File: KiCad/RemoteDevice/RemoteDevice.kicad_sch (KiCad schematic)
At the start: 42 parts, among them J1 CN1, J2 Antenne, Q1 Si4435, SW1 SW_MEC_5E, SW2 SW_MEC_5E, U1 STM32L041F6Px, U2 XC9140, U3 MCP6281, U4 ADT7410TRZ, U5 MCP6281, U6 RT606

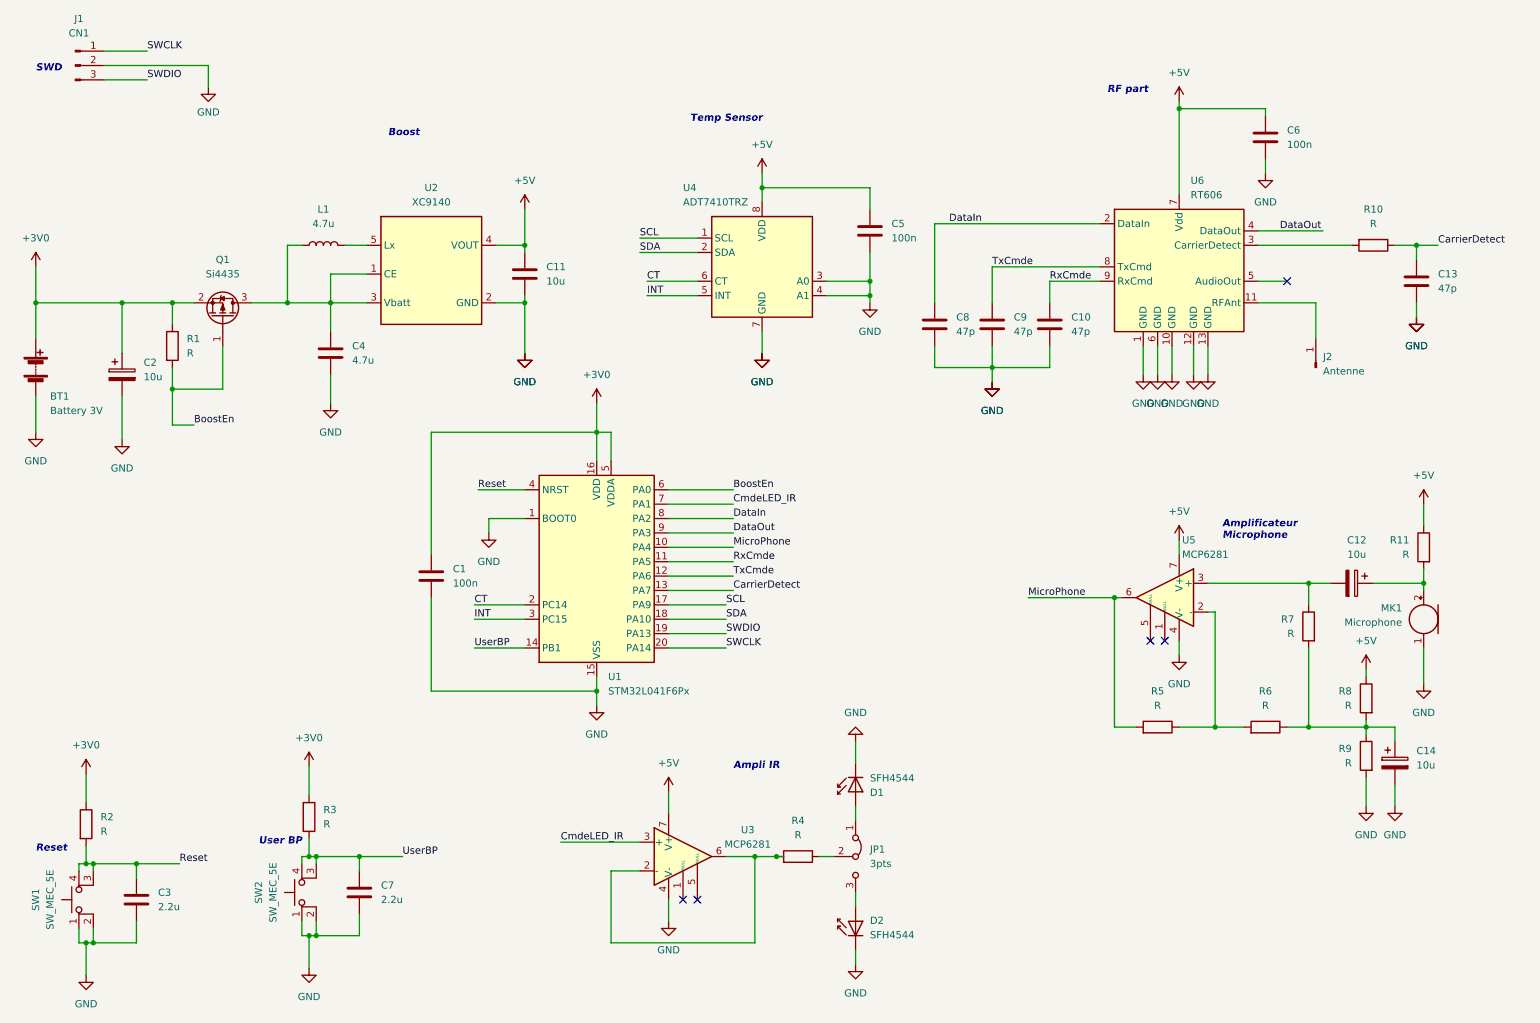
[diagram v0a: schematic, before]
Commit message: Edge cut OK, le compartiment de pile ne fait pas partie du brd (car pb en épaisseur). Placement commencé
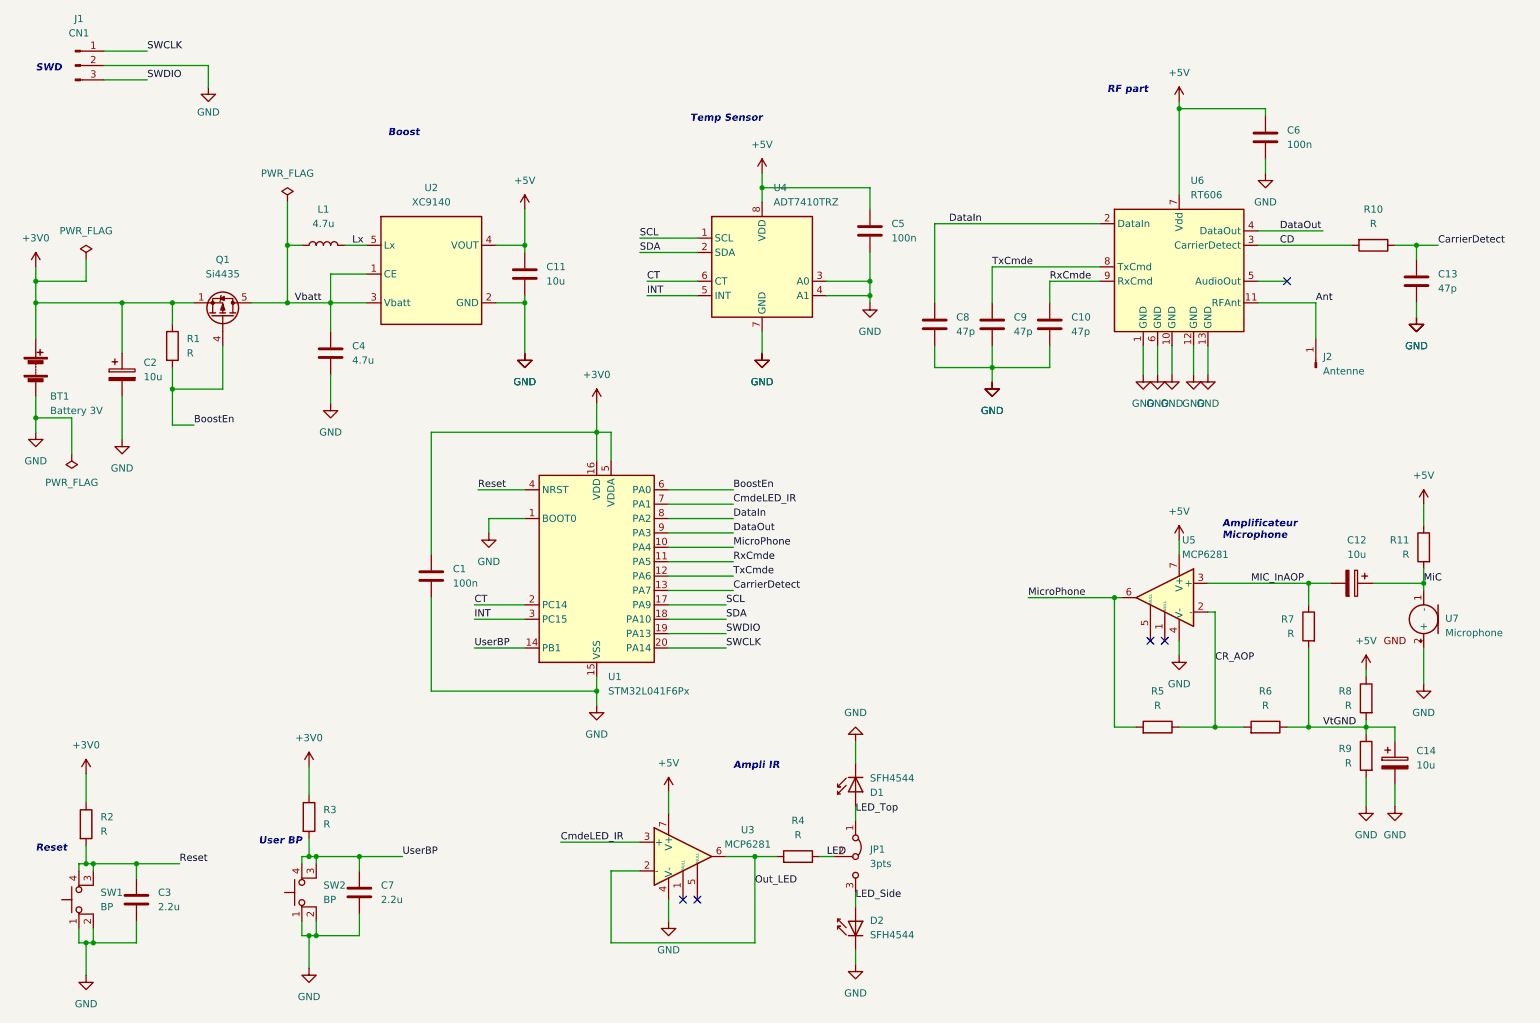
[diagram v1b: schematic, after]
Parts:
- removed MK1: Microphone, symbol Device:Microphone
- removed Q1: Si4435, symbol Device:Q_PMOS_GSD
- removed SW1, SW2: SW_MEC_5E, symbol Switch:SW_MEC_5E
- removed U2: XC9140, Package_TO_SOT_SMD:SOT-23-5, symbol ProjDeviceManag_PV:XC9140
- removed U4: ADT7410TRZ, Package_SO:SOP-8_3.9x4.9mm_P1.27mm, symbol ProjDeviceManag_PV:ADT7410TRZ
- removed U6: RT606, ProjDeviceManag_PV:RT606, symbol ProjDeviceManag_PV:RT606
- added Q1: Si4435, Package_SO:PowerPAK_SO-8_Single, symbol Transistor_FET:Si7141DP
- added SW1, SW2: BP, LibKiCad_PjtDeviceManagePV:SW, symbol LibKiCad_PjtDeviceManagePV:SwitchBP
- added U2: XC9140, Package_TO_SOT_SMD:SOT-23-5, symbol LibKiCad_PjtDeviceManagePV:XC9140
- added U4: ADT7410TRZ, Package_SO:SOP-8_3.9x4.9mm_P1.27mm, symbol LibKiCad_PjtDeviceManagePV:ADT7410TRZ
- added U6: RT606, LibKiCad_PjtDeviceManagePV:RT606, symbol LibKiCad_PjtDeviceManagePV:RT606
- added U7: Microphone, LibKiCad_PjtDeviceManagePV:Microphone, symbol LibKiCad_PjtDeviceManagePV:Microphone
- U3, U5: footprint (none) -> Package_SO:SOIC-8_3.9x4.9mm_P1.27mm
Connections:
- net +3V0: now also Q1.1 (S), Q1.2 (S), Q1.3 (S)
- net +5V: now also U2.4 (VOUT), U4.8 (VDD), U6.7 (Vdd)
- net BoostEn: now also Q1.4 (G)
- net CT: now also U4.6 (CT)
- net DataIn: now also U6.2 (DataIn)
- net DataOut: now also U6.4 (DataOut)
- net GND: now also SW1.1, SW1.2, SW2.1, SW2.2, U2.2 (GND), U4.3 (A0), U4.4 (A1), U4.7 (GND), U6.1 (GND), U6.10 (GND), U6.12 (GND), U6.13 (GND), U6.6 (GND), U7.2 (+)
- net INT: now also U4.5 (INT)
- net Reset: now also SW1.3, SW1.4
- net RxCmde: now also U6.9 (RxCmd)
- net SCL: now also U4.1 (SCL)
- net SDA: now also U4.2 (SDA)
- net TxCmde: now also U6.8 (TxCmd)
- net UserBP: now also SW2.3, SW2.4
- net LED: now reaches JP1.2 (C), R4.1
- net Out_LED: now reaches R4.2, U3.2 (-), U3.6
- net VtGND: now reaches C14.1, R6.1, R7.2, R8.2, R9.1
- net Vbatt: now reaches C4.1, L1.2
- net Vbatt: now also Q1.5 (D), U2.1 (CE), U2.3 (Vbatt)
- net Lx: now reaches L1.1
- net Lx: now also U2.5 (Lx)
- net MiC: now reaches C12.1, R11.2
- net MiC: now also U7.1 (-)
- net LED_Top: now reaches D1.2 (A), JP1.1 (A)
- net LED_Side: now reaches D2.2 (A), JP1.3 (B)
- net Ant: now reaches J2.1 (Pin_1)
- net Ant: now also U6.11 (RFAnt)
- net CD: now reaches R10.2
- net CD: now also U6.3 (CarrierDetect)
- net CR_AOP: now reaches R5.1, R6.2, U5.2 (-)
- net MIC_InAOP: now reaches C12.2, R7.1, U5.3 (+)

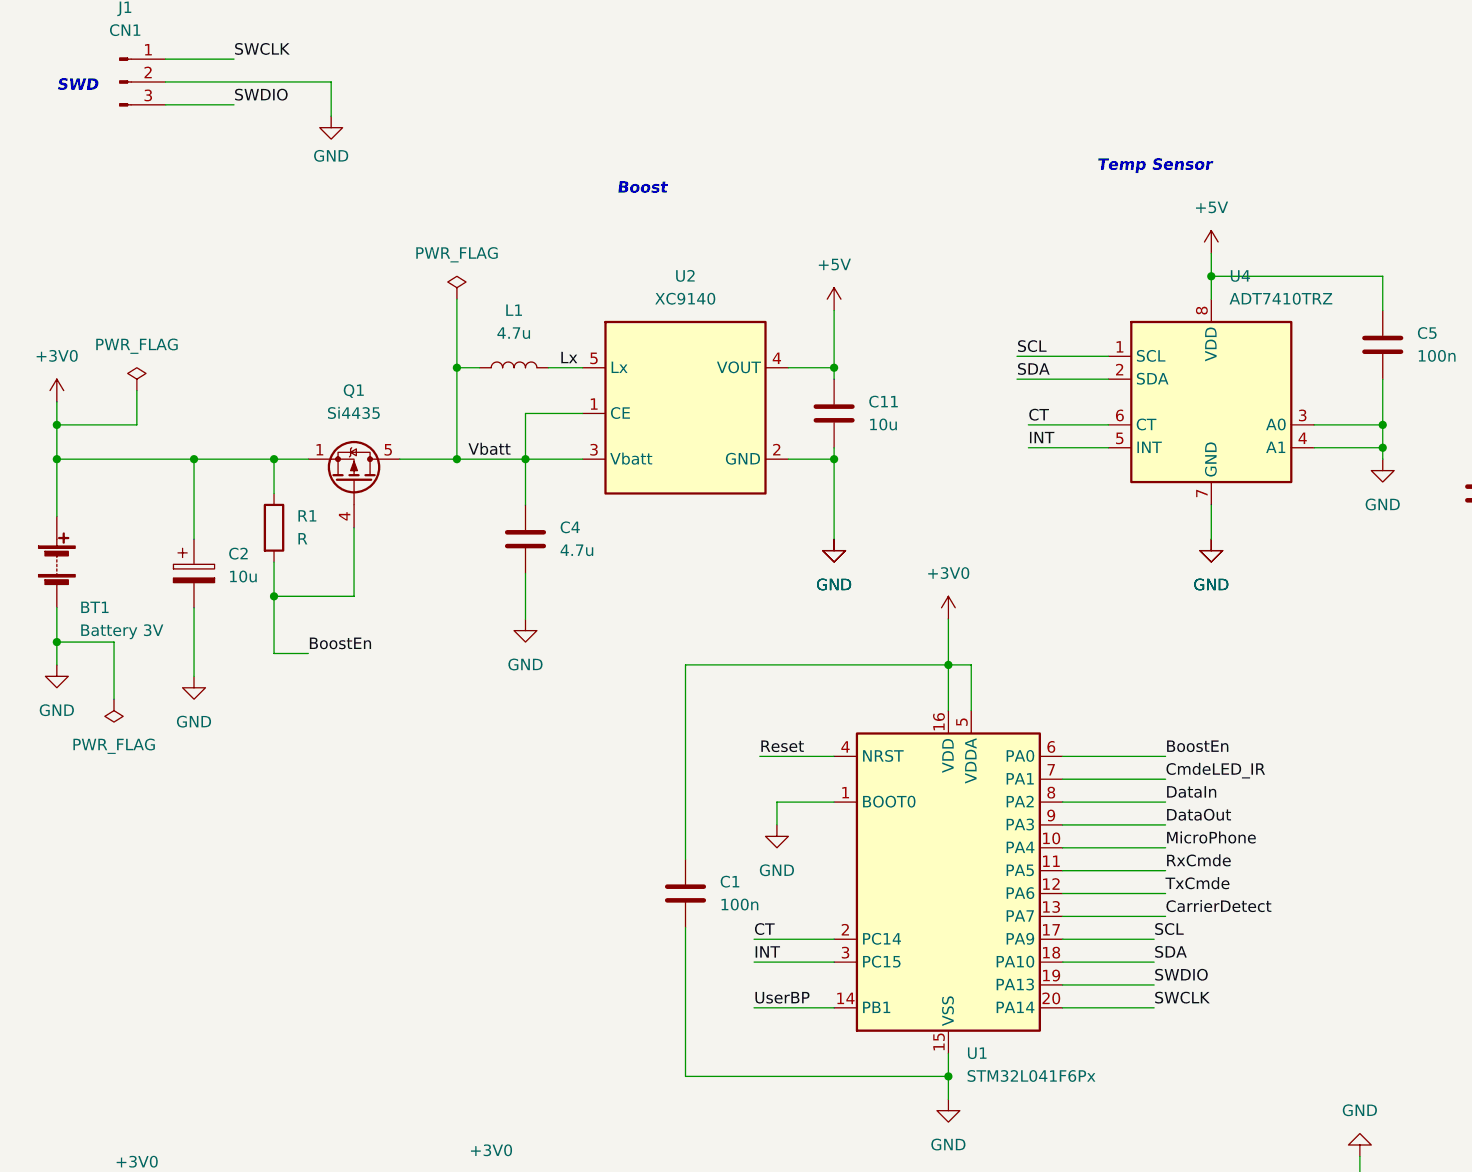
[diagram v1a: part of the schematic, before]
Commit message: routage bien avancé. Vérifier remap harmoniser odt. Reprendre pack RT606 pour passer cuivre entre pastille
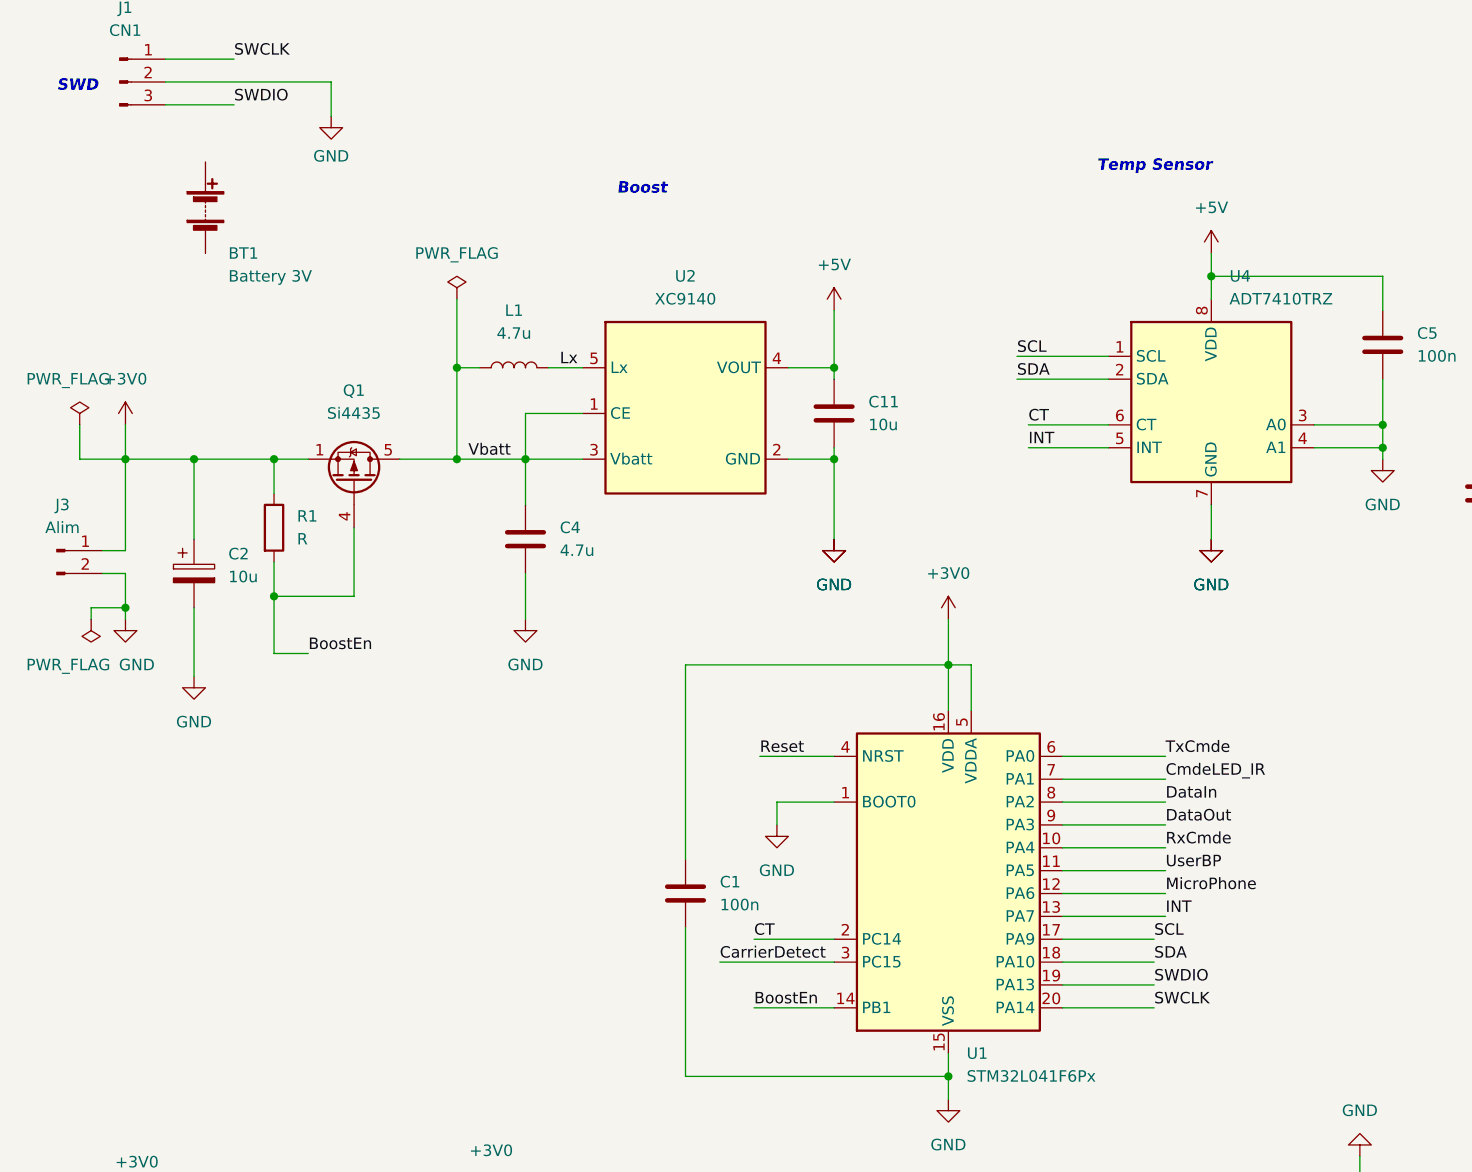
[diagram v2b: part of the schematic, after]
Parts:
- added J3: Alim, LibKiCad_PjtDeviceManagePV:PinHeader2pts, symbol Connector:Conn_01x02_Male
- J1, JP1: footprint Connector_PinHeader_2.54mm:PinHeader_1x03_P2.54mm_Vertical -> LibKiCad_PjtDeviceManagePV:PinHeader3pts
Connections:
- net +3V0: now also J3.1 (Pin_1); no longer BT1.1 (+)
- net BoostEn: now also U1.14 (PB1); no longer U1.6 (PA0)
- net CarrierDetect: now also U1.3 (PC15); no longer U1.13 (PA7)
- net GND: now also J3.2 (Pin_2); no longer BT1.2 (-)
- net INT: now also U1.13 (PA7); no longer U1.3 (PC15)
- net MicroPhone: now also U1.12 (PA6); no longer U1.10 (PA4)
- net RxCmde: now also U1.10 (PA4); no longer U1.11 (PA5)
- net TxCmde: now also U1.6 (PA0); no longer U1.12 (PA6)
- net UserBP: now also U1.11 (PA5); no longer U1.14 (PB1)
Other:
- moved on the sheet: BT1

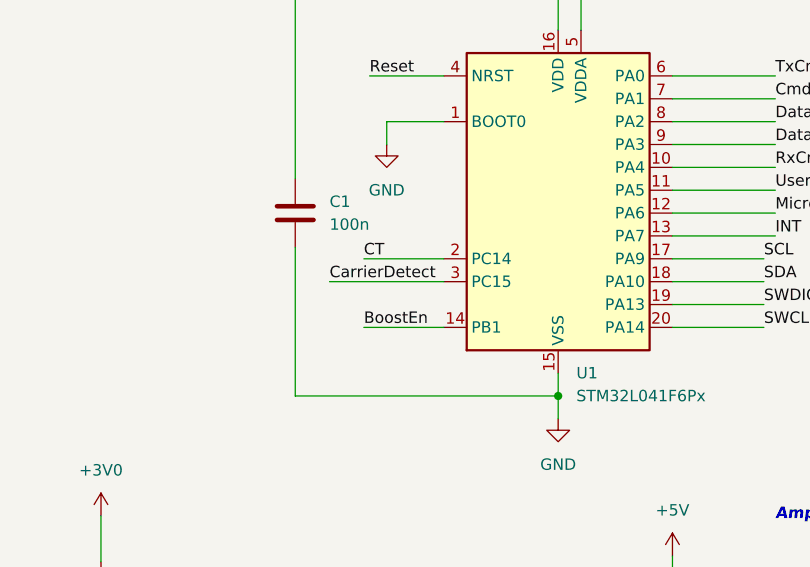
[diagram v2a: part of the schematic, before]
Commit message: paxkagez RT606 OK, remap à contrôler, routage presque entièrement dégrossi, pb DRC sur edge cut
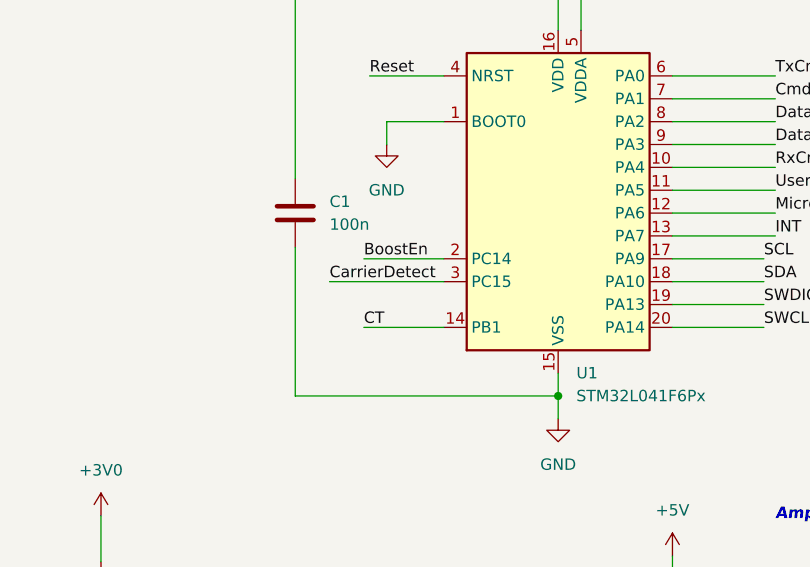
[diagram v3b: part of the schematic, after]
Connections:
- net BoostEn: now also U1.2 (PC14); no longer U1.14 (PB1)
- net CT: now also U1.14 (PB1); no longer U1.2 (PC14)
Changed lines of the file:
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@@
     (effects (font (size 1.27 1.27)) (justify left bottom))
   )
-  (label "BoostEn" (at 93.98 128.27 0)
+  (label "BoostEn" (at 93.98 120.65 0)
     (effects (font (size 1.27 1.27)) (justify left bottom))
   )
@@
     (effects (font (size 1.27 1.27)) (justify left bottom))
   )
-  (label "CT" (at 93.98 120.65 0)
+  (label "CT" (at 93.98 128.27 0)
     (effects (font (size 1.27 1.27)) (justify left bottom))
   )
